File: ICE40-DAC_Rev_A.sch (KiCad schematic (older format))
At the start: 39 parts, among them Q1 NA(BC817-40(SOT-23)), U1 THS5641AIDW(SOIC28), U2 SN74ACT244DWR(SOIC-20)

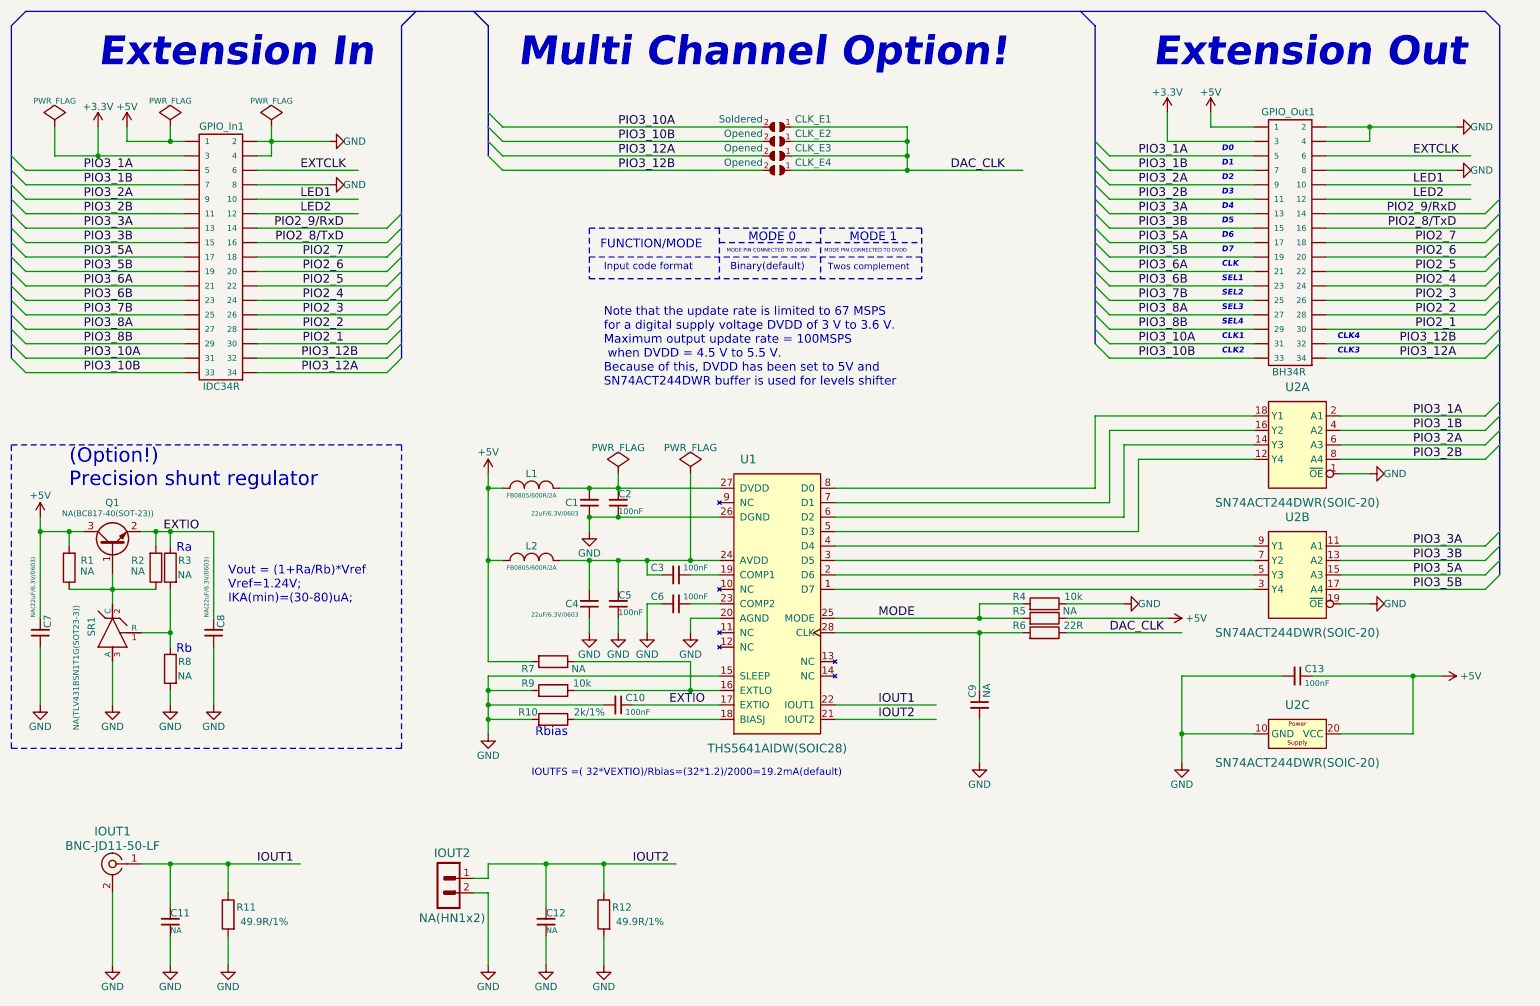
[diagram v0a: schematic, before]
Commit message: Update
Updated trace names
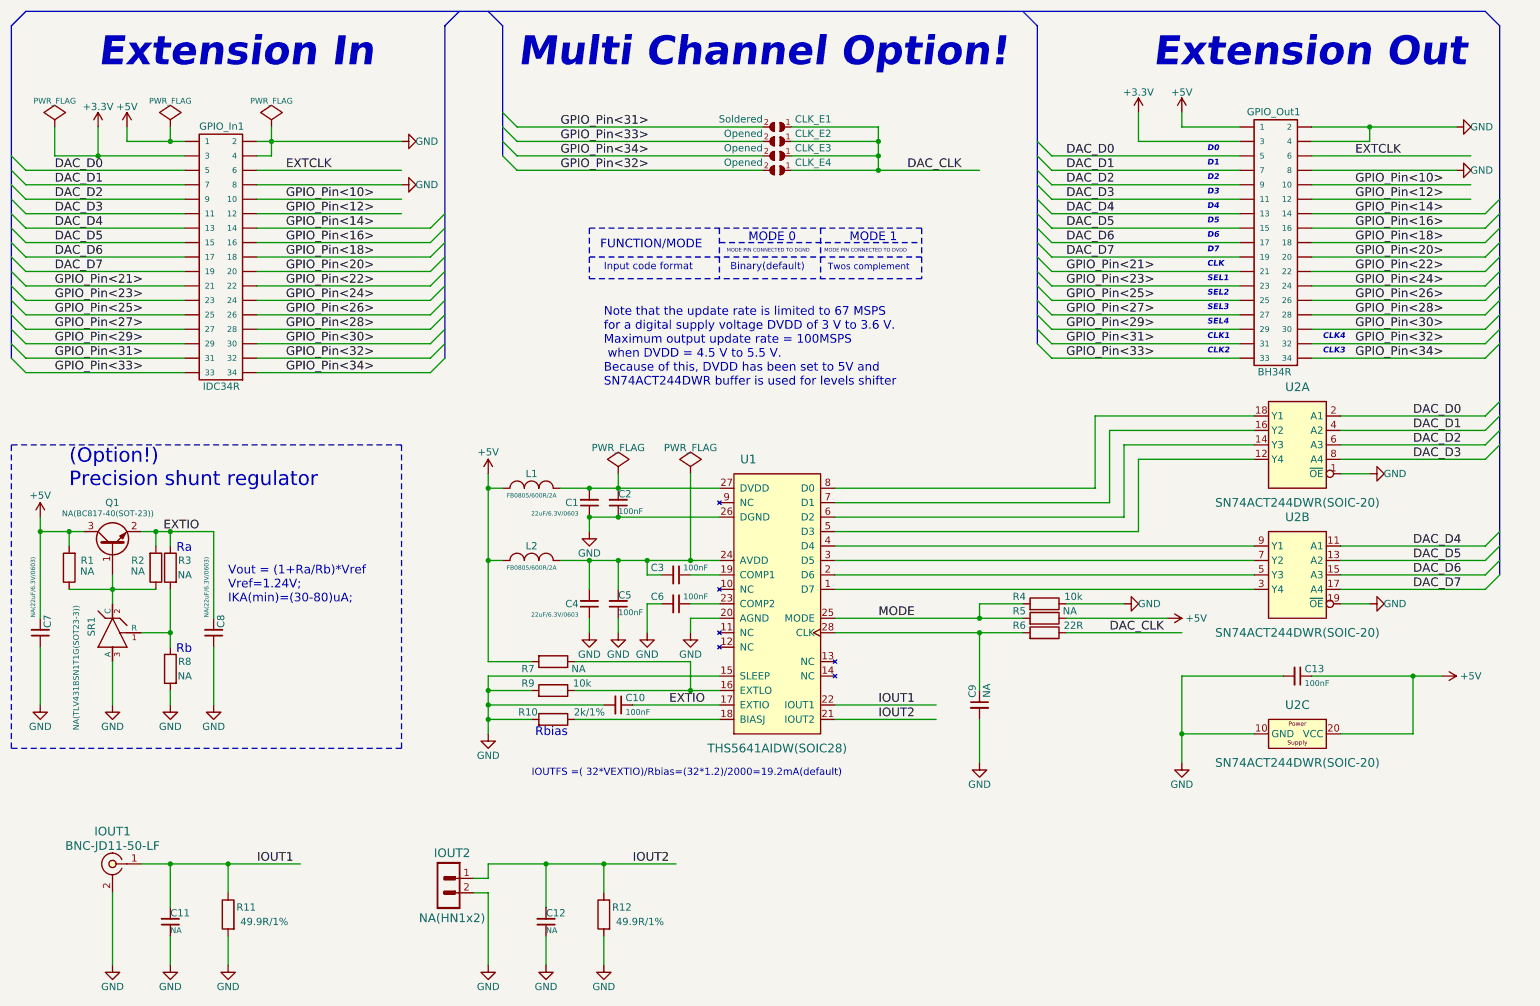
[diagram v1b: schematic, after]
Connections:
- net labels added: DAC_D0, DAC_D1, DAC_D2, DAC_D3, DAC_D4, DAC_D5, DAC_D6, DAC_D7, GPIO_Pin<10>, GPIO_Pin<12>, GPIO_Pin<14>, GPIO_Pin<16>, GPIO_Pin<18>, GPIO_Pin<20>, GPIO_Pin<21>, GPIO_Pin<22>, GPIO_Pin<23>, GPIO_Pin<24>, GPIO_Pin<25>, GPIO_Pin<26>, GPIO_Pin<27>, GPIO_Pin<28>, GPIO_Pin<29>, GPIO_Pin<30>, GPIO_Pin<31>, GPIO_Pin<32>, GPIO_Pin<33>, GPIO_Pin<34>
- net labels removed: LED1, LED2, PIO2_1, PIO2_2, PIO2_3, PIO2_4, PIO2_5, PIO2_6, PIO2_7, PIO2_8/TxD, PIO2_9/RxD, PIO3_10A, PIO3_10B, PIO3_12A, PIO3_12B, PIO3_1A, PIO3_1B, PIO3_2A, PIO3_2B, PIO3_3A, PIO3_3B, PIO3_5A, PIO3_5B, PIO3_6A, PIO3_6B, PIO3_7B, PIO3_8A, PIO3_8B
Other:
- moved on the sheet: GPIO_Out1
